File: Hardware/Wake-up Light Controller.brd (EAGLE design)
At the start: 64.1 x 49.5 mm, 37 parts, among them IC1 ST1S10, IC2 HT7333, IC3 DS3231/SO, IC4 ATMEGA328P_TQFP, J1 AVR-ISP-6PIN, Q1 BSS138, Q2 BSS138, Q3 FDN306P, Q4 FDD8447L, U1 HC_05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

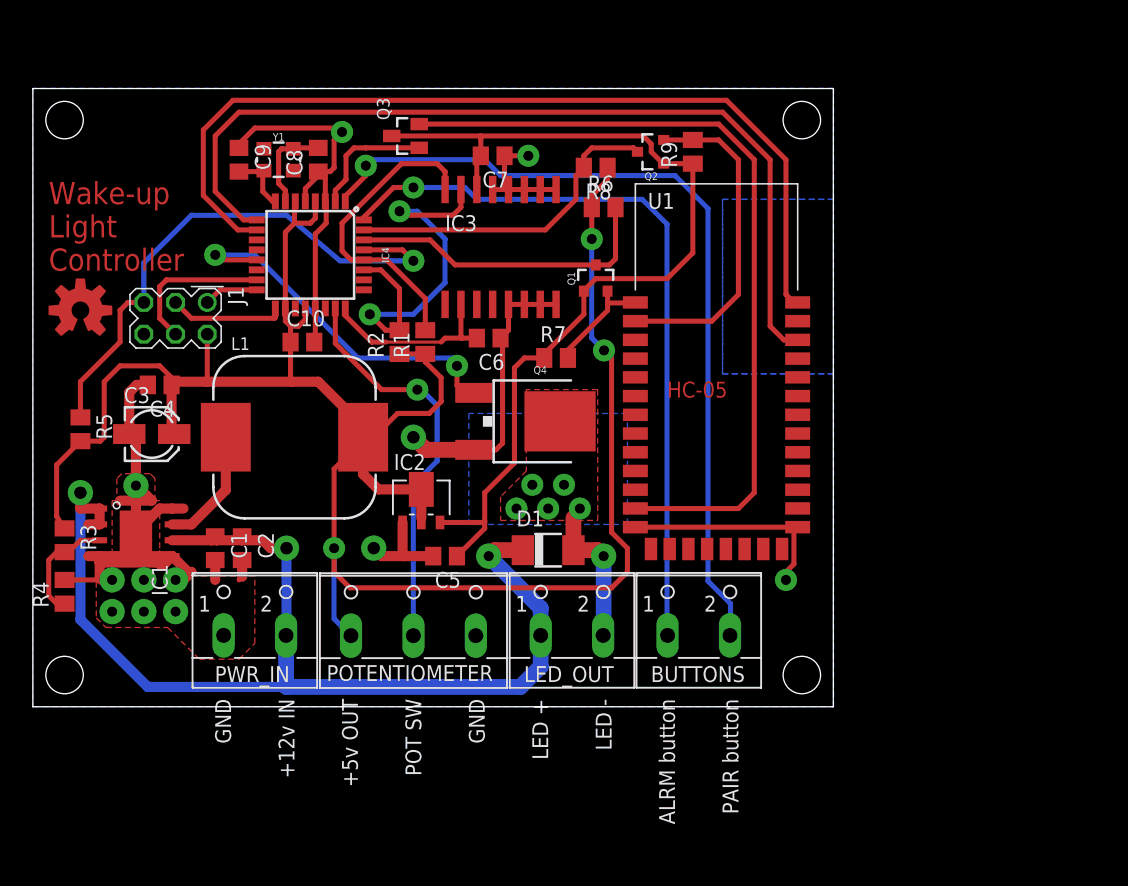
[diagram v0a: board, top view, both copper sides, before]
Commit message: Place silkscreen
Place silkscreen, and change i2c pullups to 4.7k ohm
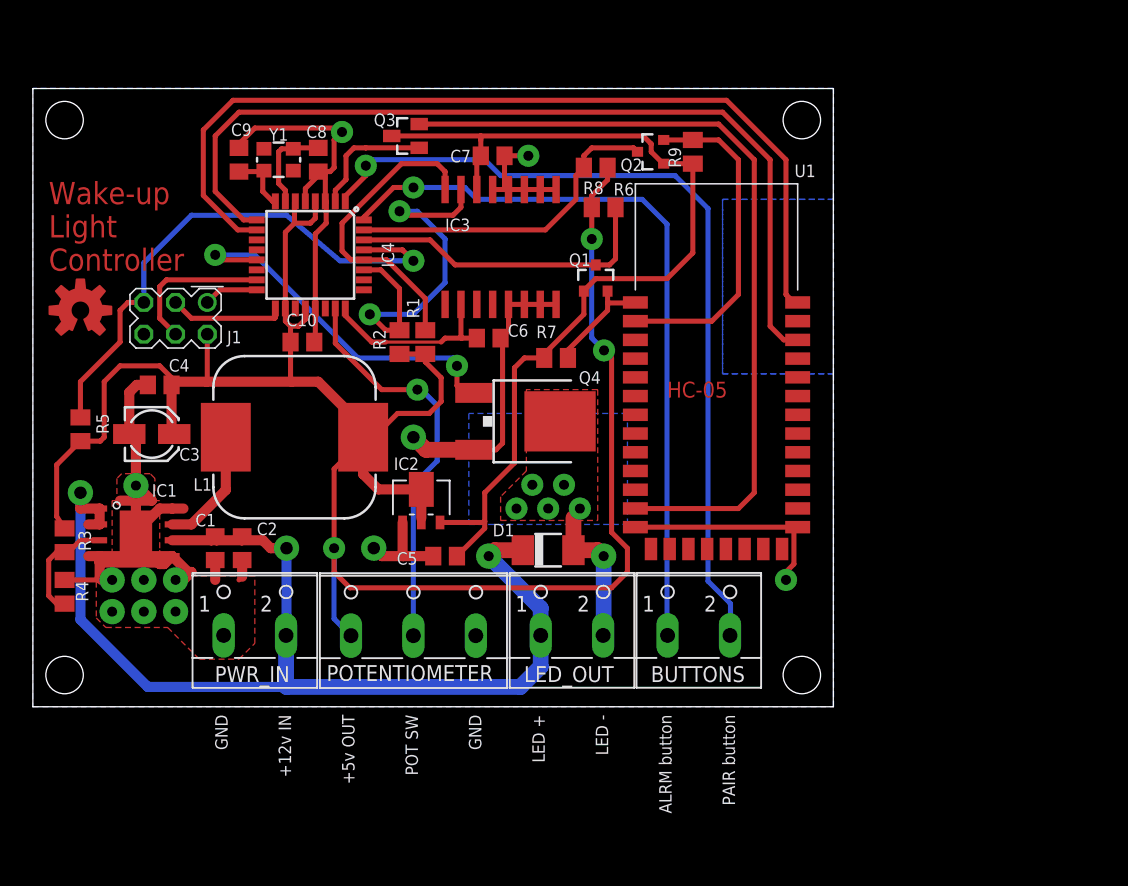
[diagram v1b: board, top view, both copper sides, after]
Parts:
- IC4: value ATMEGA328P_TQFP -> ATmega328P
- J1: value AVR-ISP-6PIN -> AVR-ISP
- R1, R2: value 10k -> 4.7k

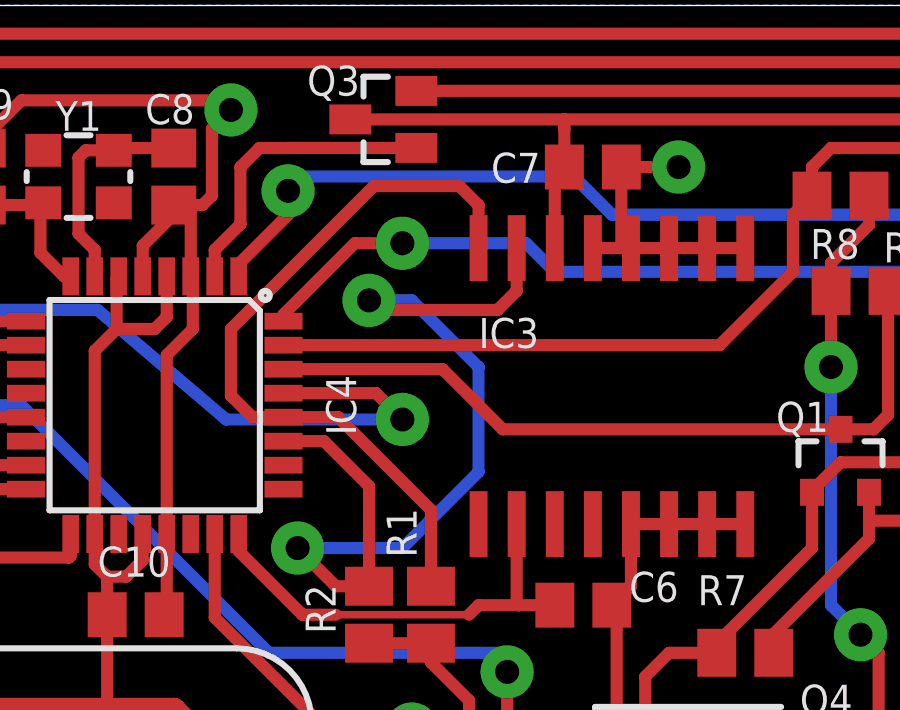
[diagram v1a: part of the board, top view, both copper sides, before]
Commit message: Reshaped one trace
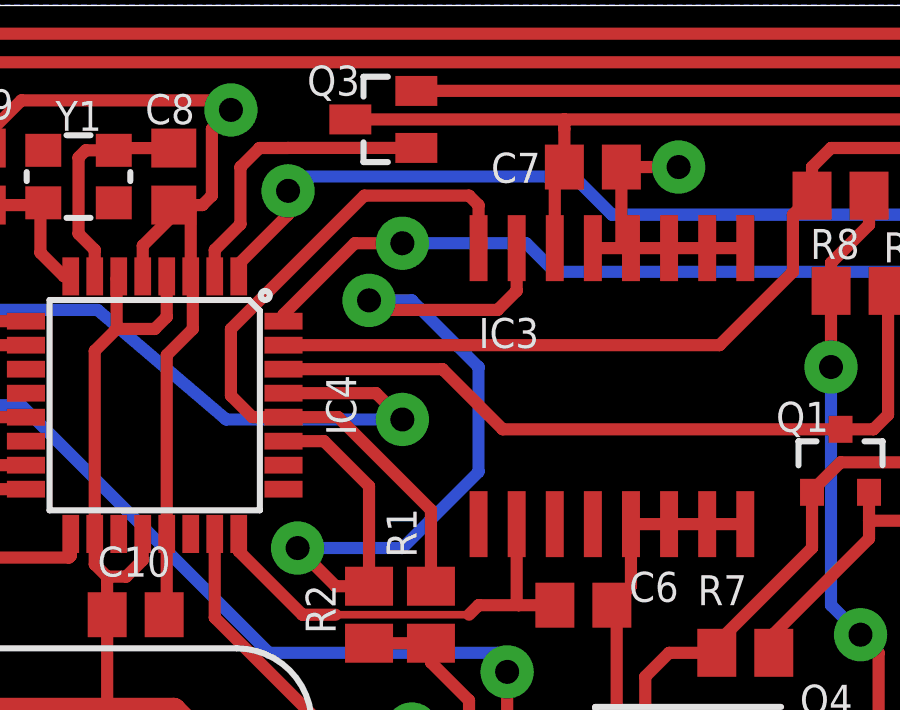
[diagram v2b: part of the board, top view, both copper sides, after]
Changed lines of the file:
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@@
 <wire x1="61.18191875" y1="13.75" x2="48.26" y2="13.75" width="0.4064" layer="1"/>
 <wire x1="61.18191875" y1="13.75" x2="61.26" y2="13.75" width="0.4064" layer="1"/>
-<wire x1="39.37" y1="31.595" x2="38.1" y2="31.595" width="0.4064" layer="1"/>
+<wire x1="38.1" y1="31.595" x2="39.37" y2="31.595" width="0.4064" layer="1"/>
 <wire x1="39.37" y1="31.595" x2="40.64" y2="31.595" width="0.4064" layer="1"/>
 <wire x1="40.64" y1="31.595" x2="41.91" y2="31.595" width="0.4064" layer="1"/>
@@
 <wire x1="22.625" y1="31.2674" x2="22.625" y2="28.66" width="0.4064" layer="1"/>
 <wire x1="22.625" y1="28.66" x2="22.54" y2="28.575" width="0.4064" layer="1"/>
+<wire x1="41.91" y1="31.595" x2="41.91" y2="40.795" width="0" layer="19" extent="1-1"/>
+<wire x1="29.615" y1="14.125" x2="31.49" y2="19.945" width="0" layer="19" extent="1-1"/>
+<wire x1="35.48" y1="5.06" x2="32.07" y2="11.43" width="0" layer="19" extent="1-1"/>
+<wire x1="16.764" y1="11.115" x2="27.305" y2="12.07093125" width="0" layer="19" extent="1-1"/>
+<wire x1="14.605" y1="9.525" x2="16.51" y2="9.525" width="0" layer="19" extent="1-1"/>
+<wire x1="12.7" y1="10.16" x2="14.605" y2="9.525" width="0" layer="19" extent="1-1"/>
+<wire x1="6.35" y1="9.525" x2="6.67" y2="9.5225" width="0" layer="19" extent="1-1"/>
+<wire x1="8.89" y1="9.525" x2="10.16" y2="10.795" width="0" layer="19" extent="1-1"/>
+<wire x1="6.35" y1="6.985" x2="6.985" y2="9.2075" width="0" layer="19" extent="1-1"/>
+<wire x1="11.43" y1="6.985" x2="11.43" y2="9.525" width="0" layer="19" extent="1-1"/>
+<wire x1="8.89" y1="6.985" x2="8.89" y2="9.525" width="0" layer="19" extent="1-1"/>
+<wire x1="8.255" y1="13.335" x2="10.038325" y2="10.916675" width="0" layer="19" extent="1-1"/>
+<wire x1="8.89" y1="29.21" x2="9.21" y2="25.146" width="0" layer="19" extent="1-1"/>
+<wire x1="15.28" y1="5.08" x2="11.43" y2="6.985" width="0" layer="19" extent="1-1"/>
+<wire x1="22.625" y1="28.66" x2="30.48" y2="20.955" width="0" layer="19" extent="1-1"/>
+<wire x1="48.26" y1="13.75" x2="37.62375" y2="20.47875" width="0" layer="19" extent="1-1"/>
 </signal>
 <signal name="+12V">
@@
 <wire x1="33.02" y1="41.275" x2="33.02" y2="40.795" width="0.4064" layer="1"/>
 <wire x1="33.02" y1="40.795" x2="33.02" y2="42.2275" width="0.4064" layer="1"/>
-<wire x1="33.02" y1="42.2275" x2="32.385" y2="42.8625" width="0.4064" layer="1"/>
-<wire x1="32.385" y1="42.8625" x2="29.5275" y2="42.8625" width="0.4064" layer="1"/>
-<wire x1="29.5275" y1="42.8625" x2="24.765" y2="38.1" width="0.4064" layer="1"/>
+<wire x1="33.02" y1="42.2275" x2="32.7025" y2="42.545" width="0.4064" layer="1"/>
+<wire x1="32.7025" y1="42.545" x2="29.21" y2="42.545" width="0.4064" layer="1"/>
+<wire x1="29.21" y1="42.545" x2="24.765" y2="38.1" width="0.4064" layer="1"/>
 <wire x1="28.34" y1="35.16" x2="26.5176" y2="35.16" width="0.4064" layer="1"/>
 <wire x1="31.4325" y1="29.525" x2="31.4325" y2="32.0675" width="0.4064" layer="1"/>
@@
 <contactref element="R2" pad="2"/>
 <contactref element="IC4" pad="27"/>
-<wire x1="34.29" y1="40.795" x2="34.29" y2="39.37" width="0.4064" layer="1"/>
+<wire x1="34.29" y1="39.37" x2="34.29" y2="40.795" width="0.4064" layer="1"/>
 <via x="29.36875" y="39.0525" extent="1-16" drill="0.8" diameter="1.778"/>
 <via x="26.9875" y="30.7975" extent="1-16" drill="0.8" diameter="1.778"/>

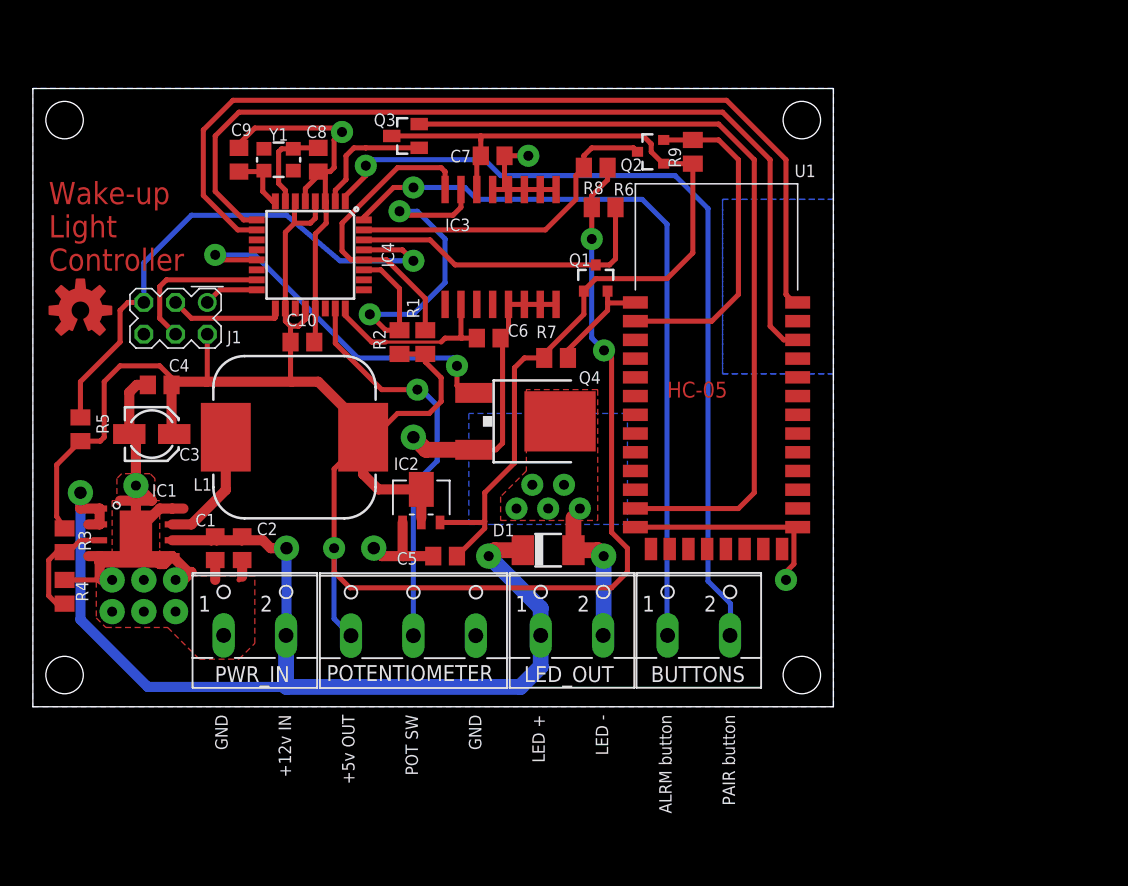
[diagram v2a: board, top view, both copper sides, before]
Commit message: REV B
Add debug function,
Add RTC battery,
Changed global layout
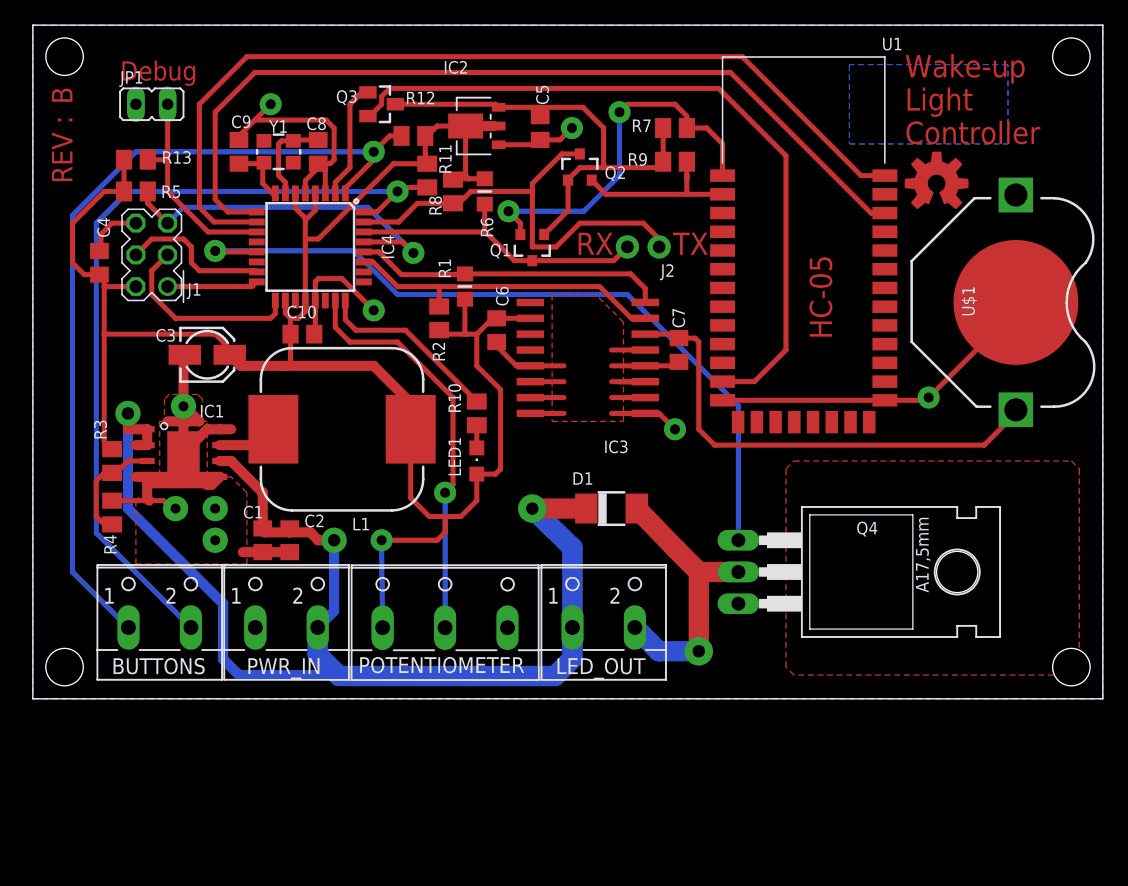
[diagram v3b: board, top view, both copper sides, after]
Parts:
- added J2: Debug, SparkFun-Connectors:1X02_NO_SILK
- added JP1: debug, jumper:JP1
- added LED1: Debug, led:CHIPLED_0805
- added R10: 330, resistor:M0805
- added R11, R12, R13: 10k, resistor:M0805
- added U$1: CR1632_3V, heol:BATTCON_16MM_PTH
- IC4: value ATmega328P -> ATMEGA328P_TQFP
- Q4: value FDD8447L -> IRLZ44N; device SparkFun-DiscreteSemi:DPAK -> transistor-power:TO220BH
- R1, R6: device resistor:M0805 -> rc-master-smd:R0805MP
- moved LOGO1 69.3 mm to (72.4, 41.3)
- moved BUTTONS 43.2 mm to (10.2, 6.99)
- moved C5 35.1 mm to (40.6, 45.7), turned to 270 degrees
- moved IC2 29.6 mm to (34.9, 45.9), turned to 90 degrees
- moved Q4 25.3 mm to (62.9, 10.2)
- moved C7 21.6 mm to (51.8, 27.9), turned to 90 degrees
- moved R7 20.7 mm to (51.4, 45.7)
- moved R5 19.6 mm to (8.26, 40.6), turned to 180 degrees
- moved U1 12.3 mm to (55.2, 41.9)
- moved R8 11.6 mm to (33.7, 40.6), turned to 270 degrees
- moved IC3 11.3 mm to (44.5, 27.3), turned to 270 degrees
- moved C4 10.9 mm to (5.33, 34.9), turned to 270 degrees
- moved R6 9.61 mm to (36.2, 40.6), turned to 270 degrees
- moved C3 7.75 mm to (14.0, 27.6)
- moved R3 7.41 mm to (6.35, 19.1)
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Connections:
- removed net RTC_PWR: C6.2, IC3.2, IC4.24
- new net DEBUG: IC4.11, JP1.2, R13.1
- new net N$3: IC4.24, R10.2
- new net N$8: LED1.C, R10.1
- new net VBAT: C7.2, IC3.14, U$1.VCC@1, U$1.VCC@2
- net +3V3: no longer C7.2, IC3.14
- net +5V: now also C4.2, C6.2, IC3.2, LED1.A, R11.1, R12.1, R13.2; no longer C4.1
- net ALRM_BTN: now also BUTTONS.2, R11.2; no longer BUTTONS.1
- net GND: now also C4.1, JP1.1, Q4.S, U$1.GND; no longer C4.2, Q4.3
- net MCU_RX: now also J2.2
- net MCU_TX: now also J2.1
- net N$1: now also Q4.D; no longer Q4.4
- net N$10: now also Q4.G; no longer Q4.1
- net PAIR_BTN: now also BUTTONS.1, R12.2; no longer BUTTONS.2
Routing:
- net +3V3: track 77.8 -> 37.5 mm
- net VBAT: track 0.00 -> 39.1 mm
- net N$10: track 29.9 -> 61.2 mm, vias 2 -> 1
- net BT_TX: track 8.91 -> 30.3 mm, vias 0 -> 2
- net DEBUG: track 0.00 -> 17.1 mm
- net RTC_PWR: track 15.4 -> 0.00 mm
- net RST: track 44.1 -> 29.2 mm
- net N$3: track 0.00 -> 14.8 mm
- net BT_RX: track 26.6 -> 13.9 mm
- net N$1: track 11.7 -> 22.5 mm, vias 6 -> 1
- net MCU_TX: track 26.4 -> 36.8 mm
- net +5V: track 170.3 -> 160.3 mm, vias 3 -> 1
- net +12V: track 91.8 -> 100.7 mm
- net N$5: track 66.0 -> 58.7 mm
- net ALRM_BTN: track 59.7 -> 66.6 mm
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- added copper zone on layer 1, net HEATSINK
- removed copper zone on layer 1, net N$1
- removed copper zone on layer 16, net N$1
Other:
- board size 64.1 x 49.5 mm -> 85.7 x 54 mm
- board text added: "B"
- board text added: "Debug"
- board text added: "REV :"
- board text added: "RX"
- board text added: "TX"
- board text removed: "+12v IN"
- board text removed: "+5v OUT"
- board text removed: "ALRM button"
- board text removed: "GND"
- board text removed: "LED +"
- board text removed: "LED -"
- board text removed: "PAIR button"
- board text removed: "POT SW"

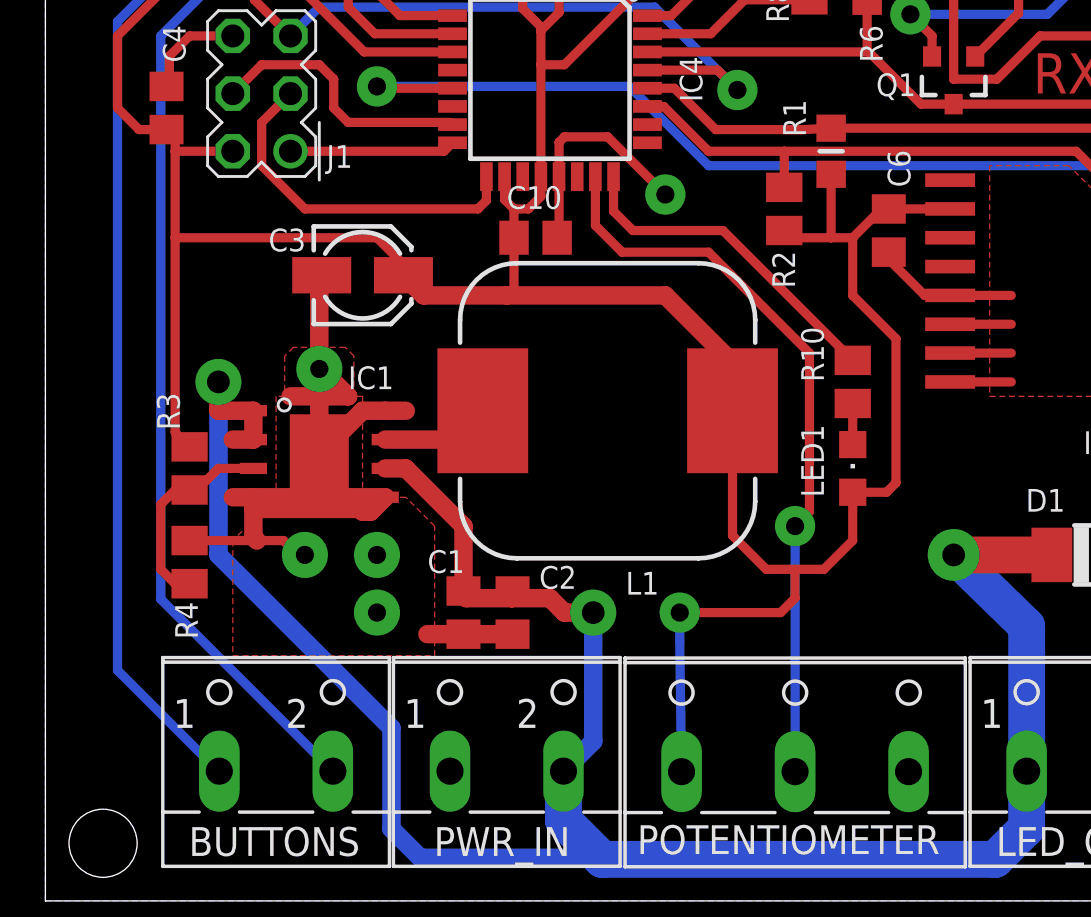
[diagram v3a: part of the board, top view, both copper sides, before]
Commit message: Add PTC fuse on 12V input
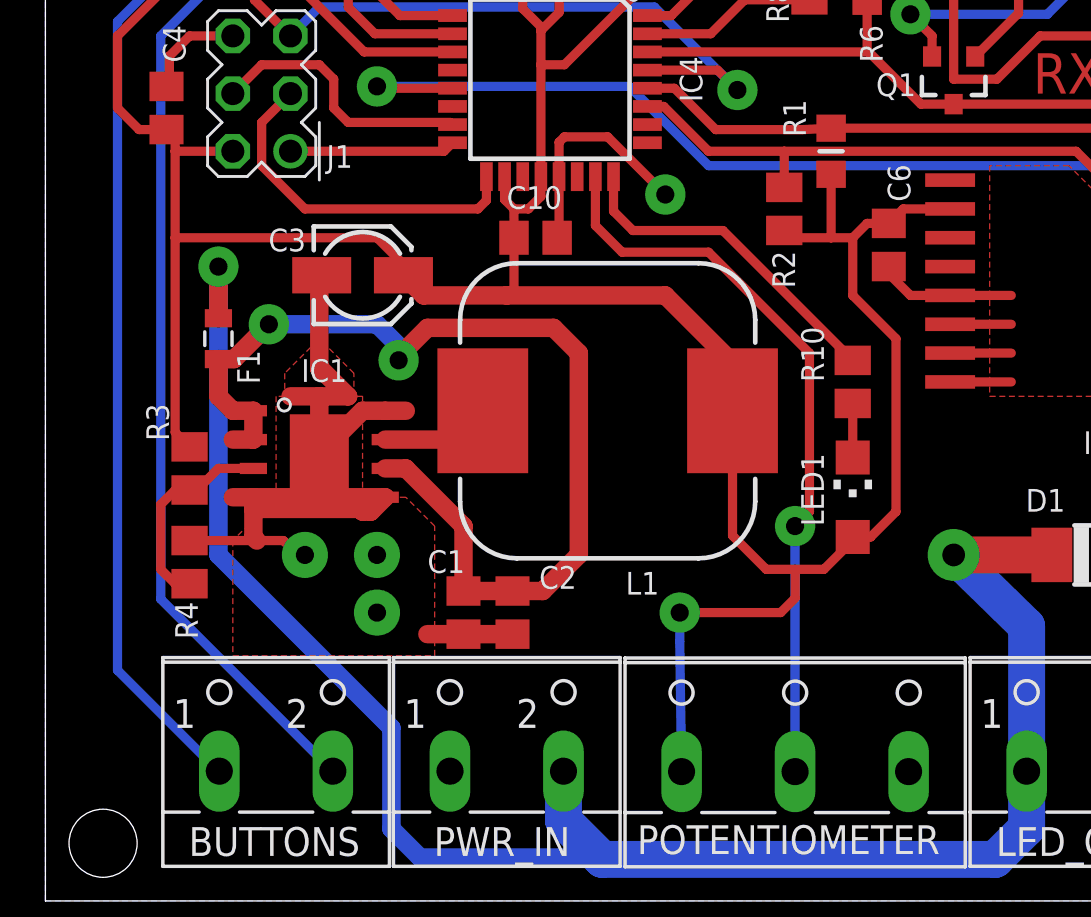
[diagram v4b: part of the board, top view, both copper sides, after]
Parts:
- added F1: PTC 500mA, BaseApp:0805-METRIC
- LED1: device led:CHIPLED_0805 -> led:CHIPLED_1206
- moved LED1 1.27 mm to (35.6, 17.8)
- moved C6 0.64 mm to (37.1, 28.9)
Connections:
- new net N$9: C1.1, C2.1, F1.2, IC1.P$1, IC1.P$2, IC1.P$6
- net +12V: now also F1.1; no longer C1.1, C2.1, IC1.P$1, IC1.P$2, IC1.P$6
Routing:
- net N$9: track 0.00 -> 46.6 mm, vias 0 -> 2
- net +12V: track 100.7 -> 81.6 mm, vias 3 -> 2
- net N$8: track 1.81 -> 2.38 mm
- net GND: track 142.5 -> 142.2 mm, vias 9 -> 8
